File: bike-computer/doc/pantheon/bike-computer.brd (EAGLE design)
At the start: 100 x 80 mm, 19 parts, among them Q1 BSS92, Q2 BSS92, T1 BC547, T2 BC547, T3 BC547

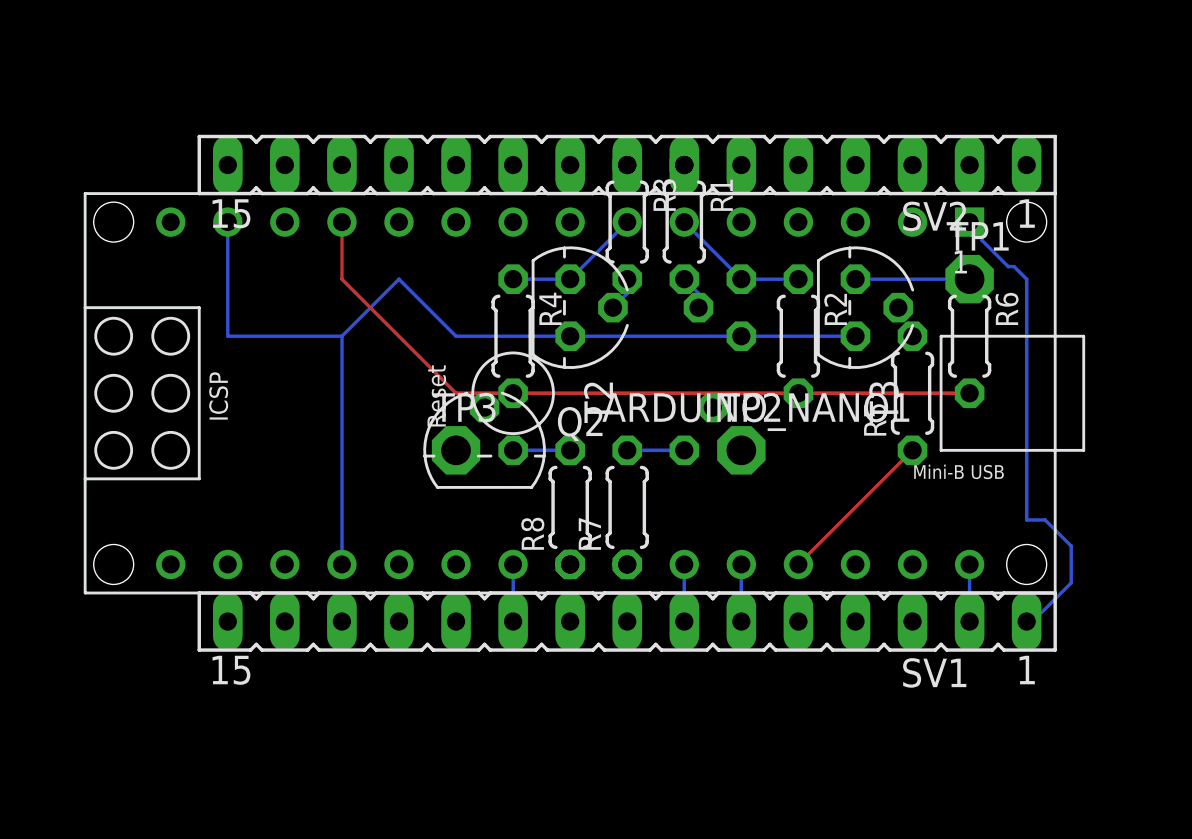
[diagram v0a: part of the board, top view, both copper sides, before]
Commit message: [Bike] Simplify speed and cadence sensors circuits.
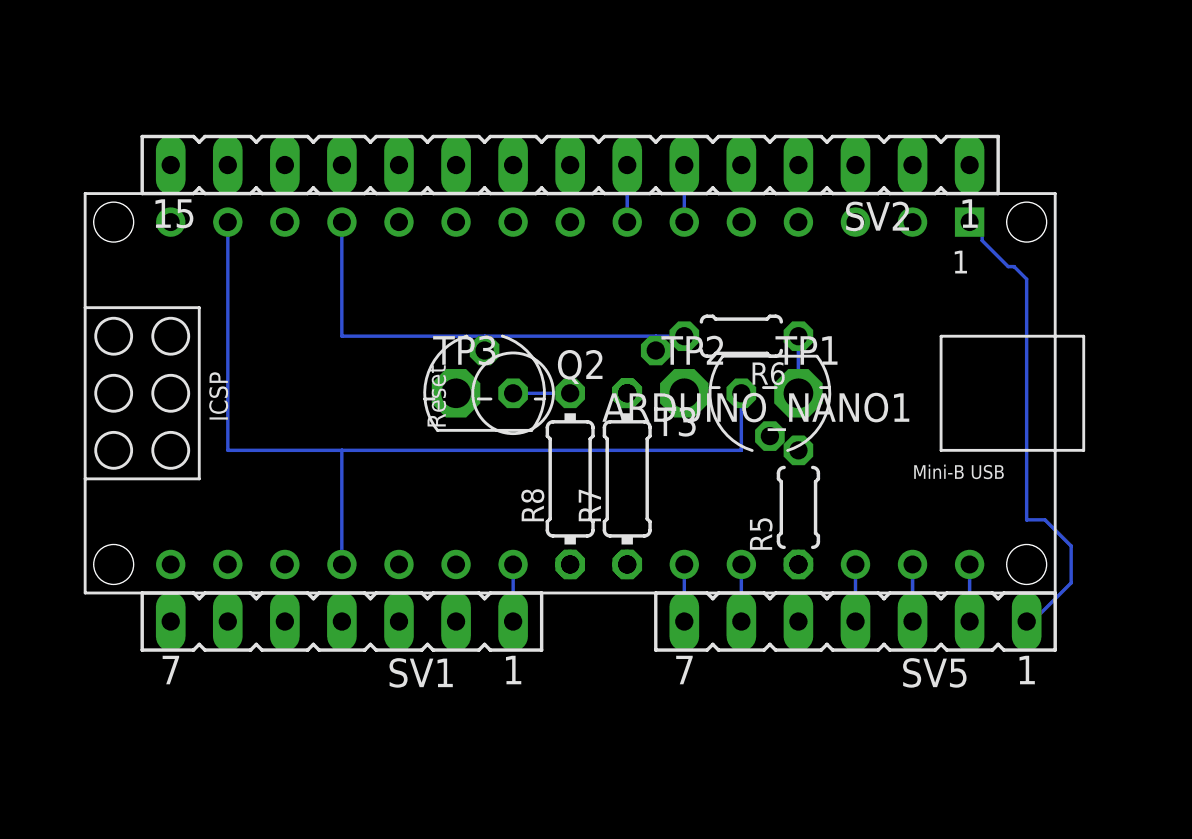
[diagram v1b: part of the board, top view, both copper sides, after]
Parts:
- removed R1, R2, R3, R4: (no value), rcl:0204/5
- removed T1, T2: BC547, transistor:TO92
- added SV5: (no value), con-lsta:FE07
- R7, R8: device rcl:0204/5 -> rcl:0204/7
- SV1: device con-lsta:FE15 -> con-lsta:FE07
- moved SV1 12.7 mm to (39.4, 30.5)
- moved R6 10.2 mm to (57.1, 43.2), turned to 180 degrees
- moved TP1 9.16 mm to (59.7, 40.6)
- moved R5 7.18 mm to (59.7, 35.6)
- moved T3 5.39 mm to (58.4, 40.6), turned to 180 degrees
- moved Q1 3.59 mm to (53.3, 40.6)
- moved TP2 3.59 mm to (54.6, 40.6)
- moved Q2 2.54 mm to (45.7, 40.6)
- moved SV2 2.54 mm to (49.5, 50.8)
- moved TP3 2.54 mm to (44.5, 40.6)
- moved R7 1.27 mm to (52.1, 36.8)
- moved R8 1.27 mm to (49.5, 36.8)
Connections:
- removed net CADENCE_SENSOR: ARDUINO_NANO1.7, R4.1, T2.3
- removed net N$1: R1.2, T1.2
- removed net N$3: R3.2, T2.2
- removed net WHEEL_SENSOR: ARDUINO_NANO1.6, R2.1, T1.3
- net +5V: no longer R2.2, R4.2
- net CADENCE_SENSOR_INPUT: now also ARDUINO_NANO1.7, SV2.7; no longer R3.1, SV2.8
- net GND: no longer T1.1, T2.1
- net MLX_CS1: now also SV5.7; no longer SV1.7
- net MLX_CS2: now also SV1.1; no longer SV1.10
- net MLX_DI: now also SV5.2; no longer SV1.2
- net MLX_RST: now also SV5.6; no longer SV1.6
- net MLX_SCK: now also SV5.1; no longer SV1.1
- net SPI_CS: now also SV5.4
- net SPI_MISO: now also SV5.3
- net WHEEL_SENSOR_INPUT: now also ARDUINO_NANO1.6, SV2.6; no longer R1.1, SV2.7
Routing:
- net +5V: track 32.6 -> 21.6 mm
- net BACKLIGHT_PWM: track 7.18 -> 0.00 mm
- net WHEEL_SENSOR: track 6.13 -> 0.00 mm
- net CADENCE_SENSOR: track 6.13 -> 0.00 mm
- net GND: track 45.3 -> 40.6 mm
- net BACKLIGHT_PWM_OUTPUT: track 5.08 -> 2.54 mm
- net SPI_MISO: track 0.00 -> 2.54 mm
- net SPI_CS: track 0.00 -> 2.54 mm
- net WHEEL_SENSOR_INPUT: track 0.00 -> 2.54 mm
- net N$5: track 2.54 -> 0.00 mm
- net CADENCE_SENSOR_INPUT: track 0.00 -> 2.54 mm
- net N$3: track 1.53 -> 0.00 mm
- net N$1: track 1.53 -> 0.00 mm

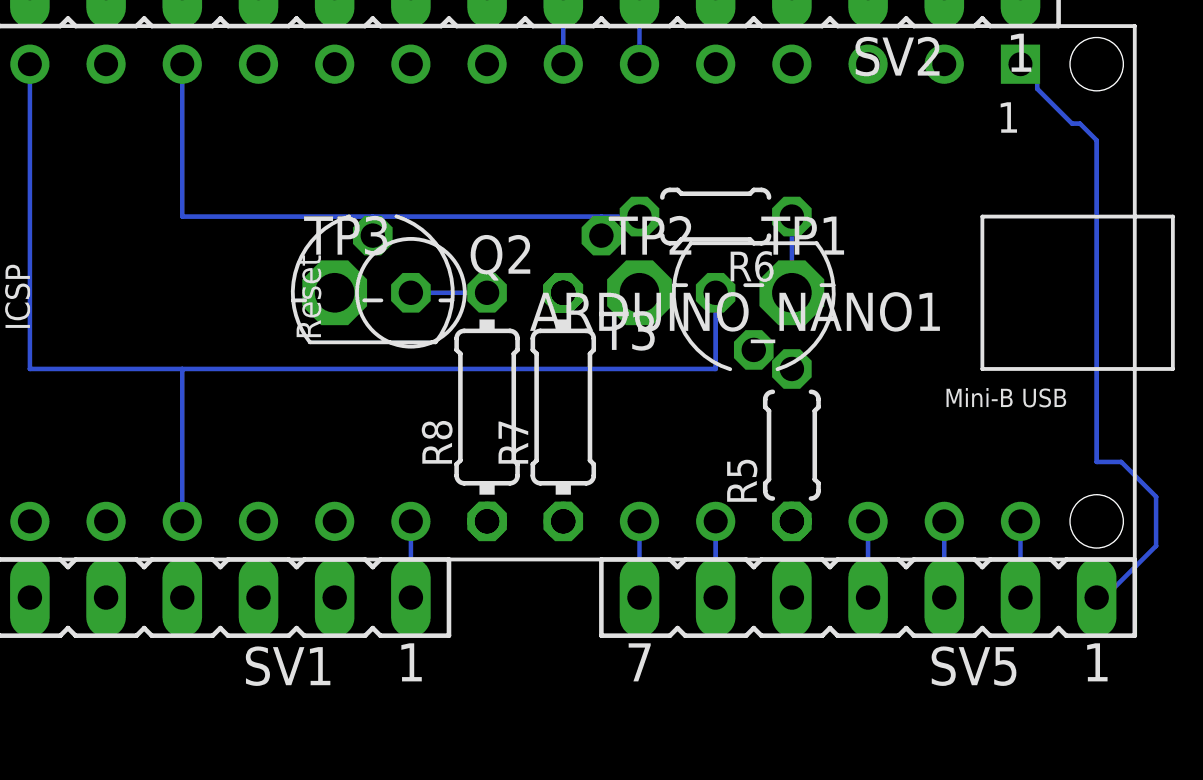
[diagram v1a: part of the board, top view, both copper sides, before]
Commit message: [Bike] Bugfix: swapped MISO and MOSI.
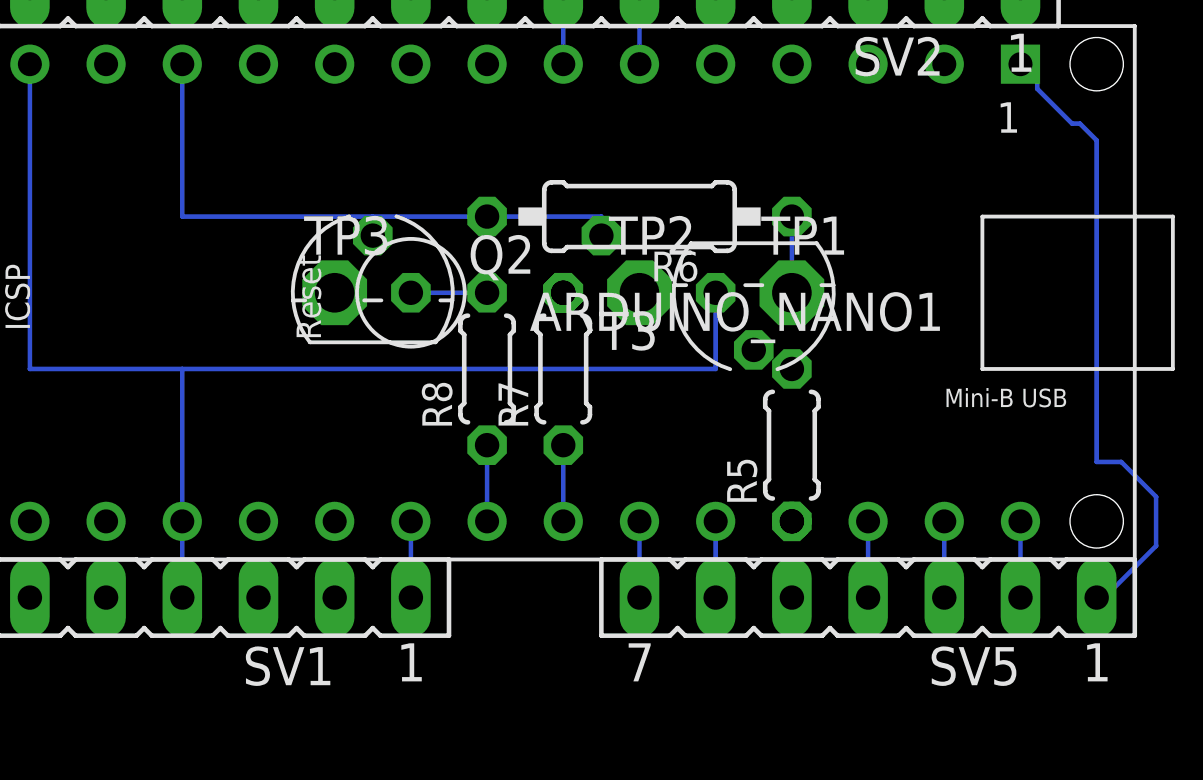
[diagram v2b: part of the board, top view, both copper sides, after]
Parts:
- R6: device rcl:0204/5 -> rcl:0207/10
- R7, R8: device rcl:0204/7 -> rcl:0204/5
- moved R6 2.54 mm to (54.6, 43.2)
- moved R7 1.27 mm to (52.1, 38.1)
- moved R8 1.27 mm to (49.5, 38.1)
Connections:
- net GND: now also SV1.4
- net MLX_DI: now also ARDUINO_NANO1.29, SV5.3; no longer ARDUINO_NANO1.30, SV5.2
- net SPI_MISO: now also ARDUINO_NANO1.30, SV5.2; no longer ARDUINO_NANO1.29, SV5.3
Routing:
- net GND: track 40.6 -> 43.2 mm
- net FRONT_LIGHT_PWM: track 0.00 -> 2.54 mm
- net BACK_LIGHT_PWM: track 0.00 -> 2.54 mm
- net +5V: track 21.6 -> 20.3 mm
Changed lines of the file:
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@@
 <attribute name="VALUE" x="62.0014" y="33.4264" size="0.9906" layer="27" ratio="10" rot="R90"/>
 </element>
-<element name="R6" library="rcl" library_urn="urn:adsk.eagle:library:334" package="0204/5" package3d_urn="urn:adsk.eagle:package:23488/1" value="" x="57.15" y="43.18" smashed="yes" rot="R180">
-<attribute name="NAME" x="59.156596875" y="42.011603125" size="0.9906" layer="25" ratio="10" rot="R180"/>
-<attribute name="POPULARITY" value="35" x="17.779996875" y="88.9" size="1.778" layer="27" rot="R180" display="off"/>
-<attribute name="SPICEPREFIX" value="R" x="17.779996875" y="88.9" size="1.778" layer="27" rot="R180" display="off"/>
-<attribute name="VALUE" x="59.283596875" y="45.4914" size="0.9906" layer="27" ratio="10" rot="R180"/>
-</element>
-<element name="R7" library="rcl" library_urn="urn:adsk.eagle:library:334" package="0204/7" package3d_urn="urn:adsk.eagle:package:23498/2" value="" x="52.07" y="36.83" smashed="yes" rot="R90">
-<attribute name="NAME" x="50.9016" y="34.8234" size="0.9906" layer="25" ratio="10" rot="R90"/>
-<attribute name="POPULARITY" value="79" x="97.79" y="83.82" size="1.778" layer="27" rot="R90" display="off"/>
-<attribute name="SPICEPREFIX" value="R" x="97.79" y="83.82" size="1.778" layer="27" rot="R90" display="off"/>
-<attribute name="VALUE" x="54.3814" y="34.6964" size="0.9906" layer="27" ratio="10" rot="R90"/>
-</element>
-<element name="R8" library="rcl" library_urn="urn:adsk.eagle:library:334" package="0204/7" package3d_urn="urn:adsk.eagle:package:23498/2" value="" x="49.53" y="36.83" smashed="yes" rot="R90">
-<attribute name="NAME" x="48.3616" y="34.8234" size="0.9906" layer="25" ratio="10" rot="R90"/>
-<attribute name="POPULARITY" value="79" x="95.25" y="91.44" size="1.778" layer="27" rot="R90" display="off"/>
-<attribute name="SPICEPREFIX" value="R" x="95.25" y="91.44" size="1.778" layer="27" rot="R90" display="off"/>
-<attribute name="VALUE" x="51.8414" y="34.6964" size="0.9906" layer="27" ratio="10" rot="R90"/>
+<element name="R6" library="rcl" library_urn="urn:adsk.eagle:library:334" package="0207/10" package3d_urn="urn:adsk.eagle:package:23491/2" value="" x="54.61" y="43.18" smashed="yes" rot="R180">
+<attribute name="NAME" x="56.616596875" y="42.011603125" size="0.9906" layer="25" ratio="10" rot="R180"/>
+<attribute name="POPULARITY" value="81" x="15.239996875" y="88.9" size="1.778" layer="27" rot="R180" display="off"/>
+<attribute name="SPICEPREFIX" value="R" x="15.239996875" y="88.9" size="1.778" layer="27" rot="R180" display="off"/>
+<attribute name="VALUE" x="56.743596875" y="45.4914" size="0.9906" layer="27" ratio="10" rot="R180"/>
+</element>
+<element name="R7" library="rcl" library_urn="urn:adsk.eagle:library:334" package="0204/5" package3d_urn="urn:adsk.eagle:package:23488/1" value="" x="52.07" y="38.1" smashed="yes" rot="R90">
+<attribute name="NAME" x="50.9016" y="36.0934" size="0.9906" layer="25" ratio="10" rot="R90"/>
+<attribute name="POPULARITY" value="35" x="97.79" y="85.09" size="1.778" layer="27" rot="R90" display="off"/>
+<attribute name="SPICEPREFIX" value="R" x="97.79" y="85.09" size="1.778" layer="27" rot="R90" display="off"/>
+<attribute name="VALUE" x="54.3814" y="35.9664" size="0.9906" layer="27" ratio="10" rot="R90"/>
+</element>
+<element name="R8" library="rcl" library_urn="urn:adsk.eagle:library:334" package="0204/5" package3d_urn="urn:adsk.eagle:package:23488/1" value="" x="49.53" y="38.1" smashed="yes" rot="R90">
+<attribute name="NAME" x="48.3616" y="36.0934" size="0.9906" layer="25" ratio="10" rot="R90"/>
+<attribute name="POPULARITY" value="35" x="95.25" y="92.71" size="1.778" layer="27" rot="R90" display="off"/>
+<attribute name="SPICEPREFIX" value="R" x="95.25" y="92.71" size="1.778" layer="27" rot="R90" display="off"/>
+<attribute name="VALUE" x="51.8414" y="35.9664" size="0.9906" layer="27" ratio="10" rot="R90"/>
 </element>
 <element name="T3" library="transistor" library_urn="urn:adsk.eagle:library:402" package="TO92" package3d_urn="urn:adsk.eagle:package:28523/2" value="BC547" x="58.42" y="40.64" smashed="yes" rot="R180">
@@
 <wire x1="34.29" y1="38.1" x2="34.29" y2="48.26" width="0.1524" layer="16"/>
 <wire x1="39.37" y1="33.02" x2="39.37" y2="38.1" width="0.1524" layer="16"/>
+<contactref element="SV1" pad="4"/>
+<wire x1="39.37" y1="30.48" x2="39.37" y2="33.02" width="0.1524" layer="16"/>
 </signal>
 <signal name="VIN">
@@
 </signal>
 <signal name="MLX_DI">
-<contactref element="ARDUINO_NANO1" pad="30"/>
-<contactref element="SV5" pad="2"/>
-<wire x1="67.31" y1="30.48" x2="67.31" y2="33.02" width="0.1524" layer="16"/>
+<contactref element="ARDUINO_NANO1" pad="29"/>
+<contactref element="SV5" pad="3"/>
+<wire x1="64.77" y1="33.02" x2="64.77" y2="30.48" width="0.1524" layer="16"/>
 </signal>
 <signal name="MLX_SCK">
@@
 <contactref element="ARDUINO_NANO1" pad="24"/>
 <contactref element="R7" pad="1"/>
+<wire x1="52.07" y1="35.56" x2="52.07" y2="33.02" width="0.1524" layer="16"/>
 </signal>
 <signal name="BACK_LIGHT_PWM">
 <contactref element="ARDUINO_NANO1" pad="23"/>
 <contactref element="R8" pad="1"/>
+<wire x1="49.53" y1="35.56" x2="49.53" y2="33.02" width="0.1524" layer="16"/>
 </signal>
 <signal name="+5V">
@@
 <wire x1="39.37" y1="48.26" x2="39.37" y2="43.18" width="0.1524" layer="16"/>
 <wire x1="39.37" y1="43.18" x2="45.72" y2="43.18" width="0.1524" layer="16"/>
-<wire x1="45.72" y1="43.18" x2="53.34" y2="43.18" width="0.1524" layer="16"/>
-<wire x1="53.34" y1="43.18" x2="54.61" y2="43.18" width="0.1524" layer="16"/>
+<wire x1="45.72" y1="43.18" x2="49.53" y2="43.18" width="0.1524" layer="16"/>
+<wire x1="53.34" y1="43.18" x2="49.53" y2="43.18" width="0.1524" layer="16"/>
 <wire x1="45.72" y1="42.545" x2="45.72" y2="43.18" width="0.1524" layer="16"/>
 <wire x1="53.34" y1="42.545" x2="53.34" y2="43.18" width="0.1524" layer="16"/>
@@
 </signal>
 <signal name="SPI_MISO">
-<contactref element="ARDUINO_NANO1" pad="29"/>
-<contactref element="SV5" pad="3"/>
-<wire x1="64.77" y1="30.48" x2="64.77" y2="33.02" width="0.1524" layer="16"/>
+<contactref element="ARDUINO_NANO1" pad="30"/>
+<contactref element="SV5" pad="2"/>
+<wire x1="67.31" y1="33.02" x2="67.31" y2="30.48" width="0.1524" layer="16"/>
 </signal>
 <signal name="SPI_CS">
